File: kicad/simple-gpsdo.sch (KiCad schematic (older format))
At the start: 100 parts, among them J1 PPS_OUT, J2 PWR, J3 ISP, J4 GPS_NEO, J5 GPS_IN, J6 10MHz_OUT, J7 NEO-6M, J8 10MHz_OUT, J9 USB_C, Q1 DMP3099L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

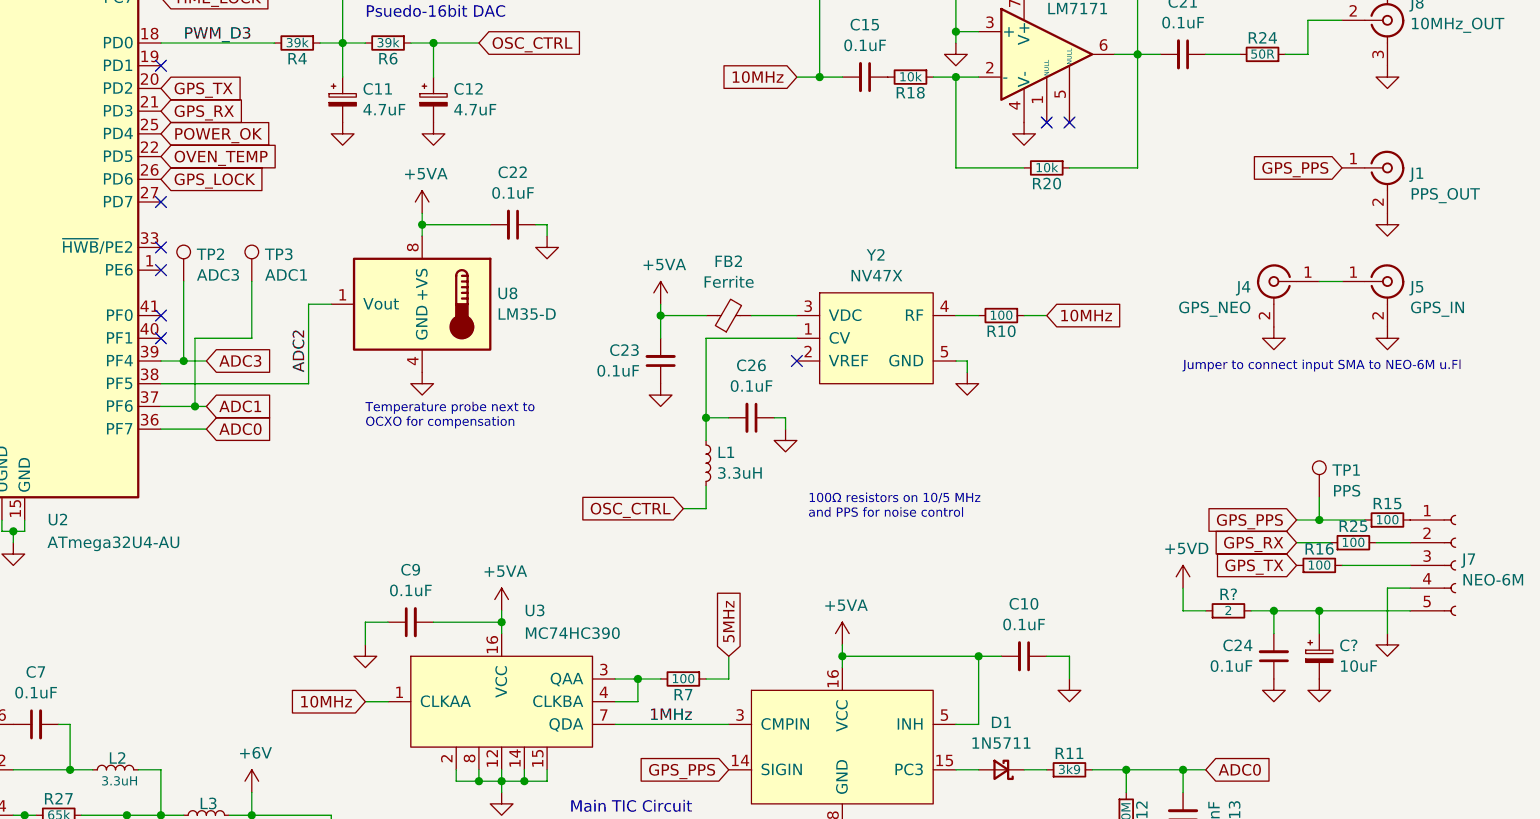
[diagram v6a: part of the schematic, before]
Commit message: added filtering to LM35
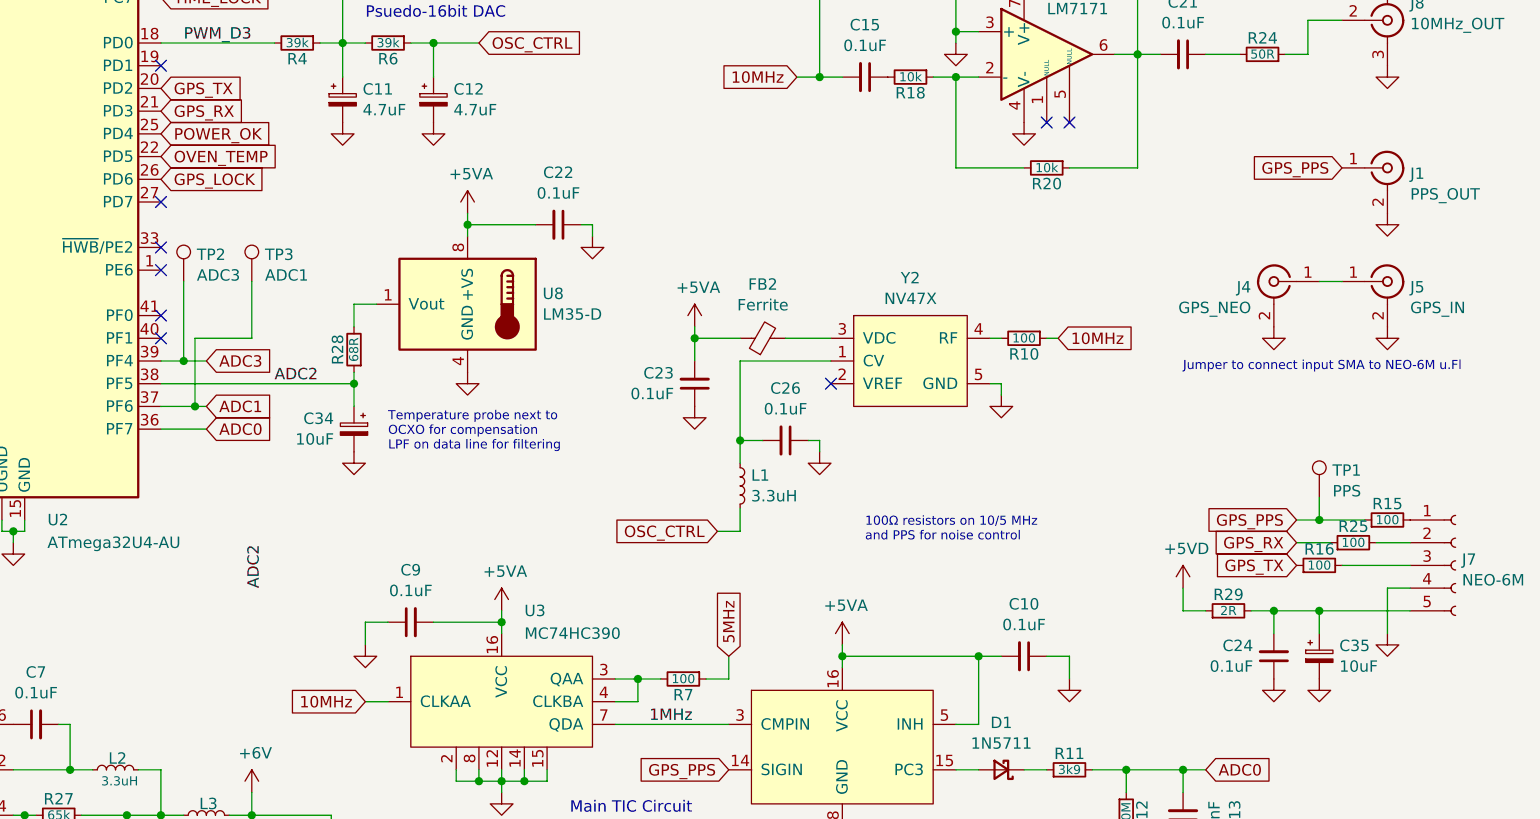
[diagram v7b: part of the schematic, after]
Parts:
- added C34: 10uF, Capacitor_SMD:C_1206_3216Metric_Pad1.42x1.75mm_HandSolder, symbol Device:CP_Small
- added R28: 68R, Resistor_SMD:R_0805_2012Metric_Pad1.15x1.40mm_HandSolder, symbol Device:R_Small
- R29: renamed from R?; value 2 -> 2R
- gave numbers to parts that had none: 1
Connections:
- net ADC2: now also C34.1, R28.1; no longer U8.1 (Vout)
- net GND: now also C34.2
- new net: R28.2, U8.1 (Vout)
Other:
- note added: "Temperature probe next to\nOCXO for compensation\nLPF on data line for filtering"
- note removed: "Temperature probe next to\nOCXO for compensation"
- moved on the sheet: C22, C23, C26, FB2, L1, R10, U8, Y2

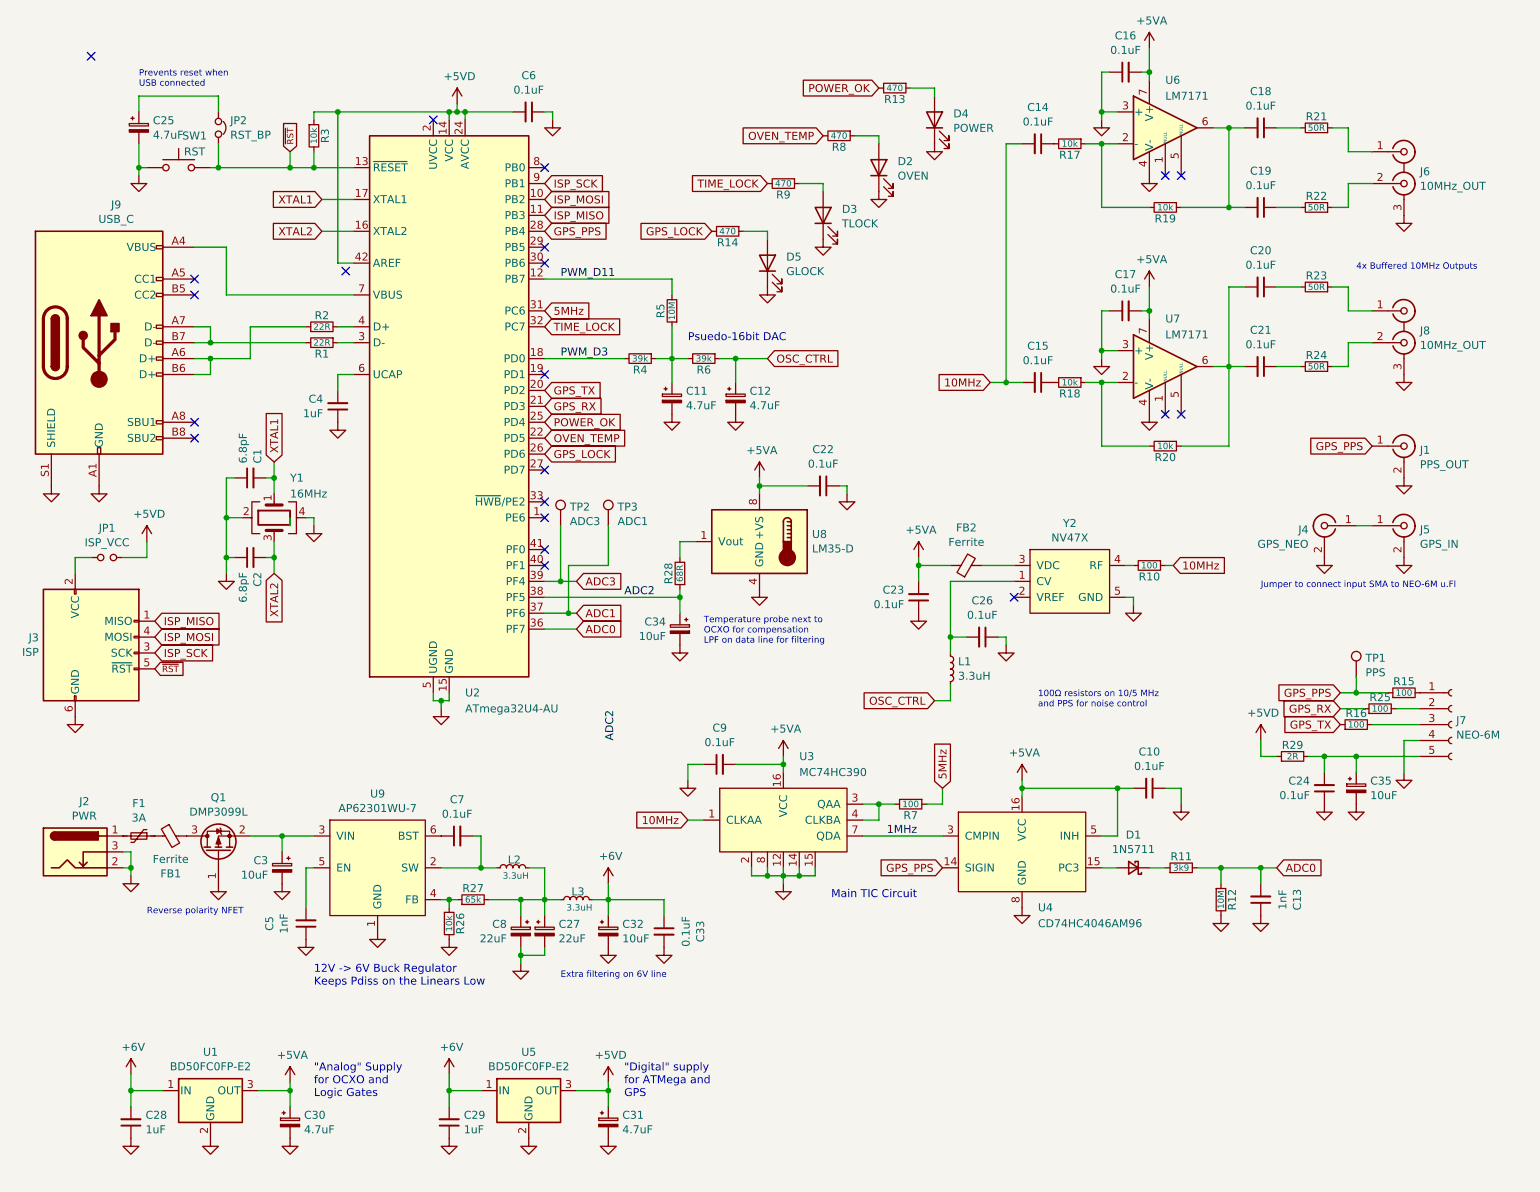
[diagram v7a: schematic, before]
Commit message: added fan control to schematic, board work still needed
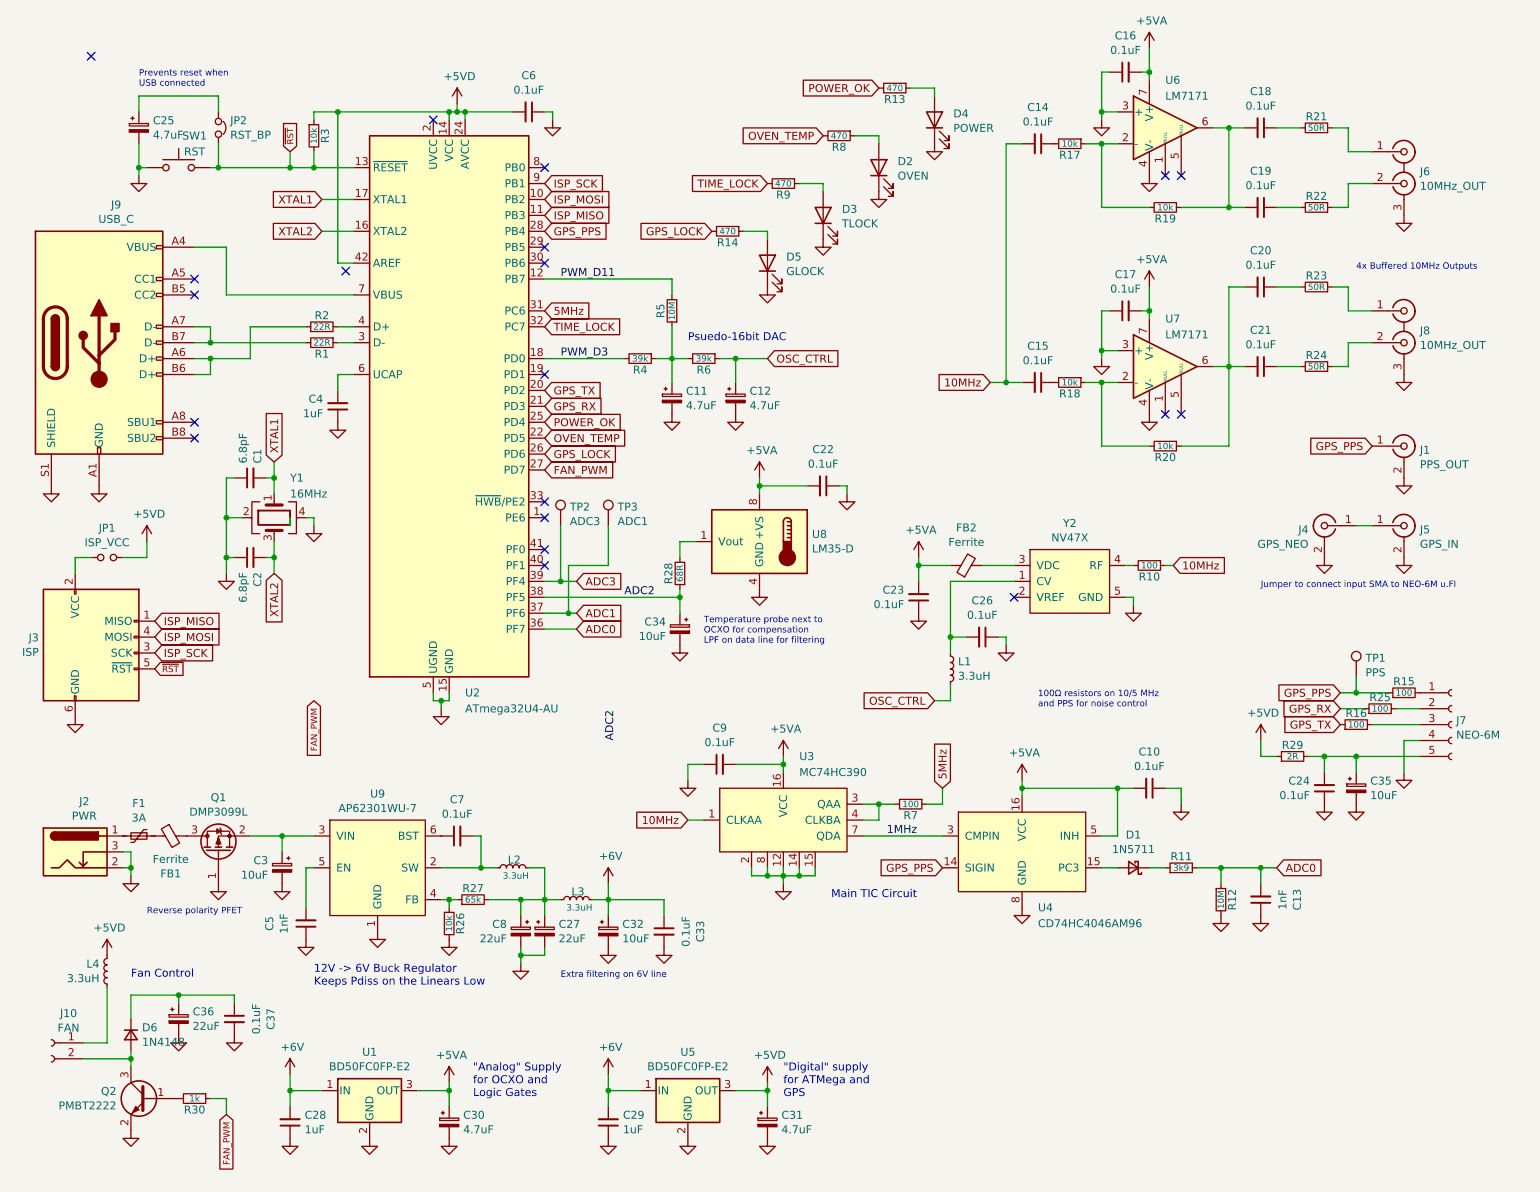
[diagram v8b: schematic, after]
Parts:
- added C36: 22uF, Capacitor_SMD:C_1206_3216Metric_Pad1.42x1.75mm_HandSolder, symbol Device:CP_Small
- added C37: 0.1uF, Capacitor_SMD:C_0805_2012Metric_Pad1.15x1.40mm_HandSolder, symbol Device:C_Small
- added D6: 1N4148, Diode_SMD:D_SOD-123, symbol Device:D_Small
- added J10: FAN, Connector_PinHeader_2.54mm:PinHeader_1x02_P2.54mm_Vertical, symbol Connector:Conn_01x02_Female
- added L4: 3.3uH, Inductor_SMD:L_1206_3216Metric_Pad1.42x1.75mm_HandSolder, symbol Device:L_Small
- added Q2: PMBT2222, Package_TO_SOT_SMD:SOT-23_Handsoldering, symbol Device:Q_NPN_BEC
- added R30: 1k, Resistor_SMD:R_0805_2012Metric_Pad1.15x1.40mm_HandSolder, symbol Device:R_Small
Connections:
- net +5VD: now also L4.1
- net GND: now also C36.2, C37.2, Q2.2 (E)
- net FAN_PWM: now reaches U2.27 (PD7)
- net FAN_PWM: now also R30.1
- new net: Q2.1 (B), R30.2
- new net: D6.2 (A), J10.2 (Pin_2), Q2.3 (C)
- new net: C36.1, C37.1, D6.1 (K)
- new net: J10.1 (Pin_1), L4.2
- no-connect marks 21 -> 20
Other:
- note added: "Fan Control"
- note added: "Reverse polarity PFET"
- note removed: "Reverse polarity NFET"
- moved on the sheet: C28, C29, C30, C31, U1, U5
